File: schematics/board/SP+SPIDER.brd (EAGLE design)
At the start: 82 x 100 mm, 45 parts

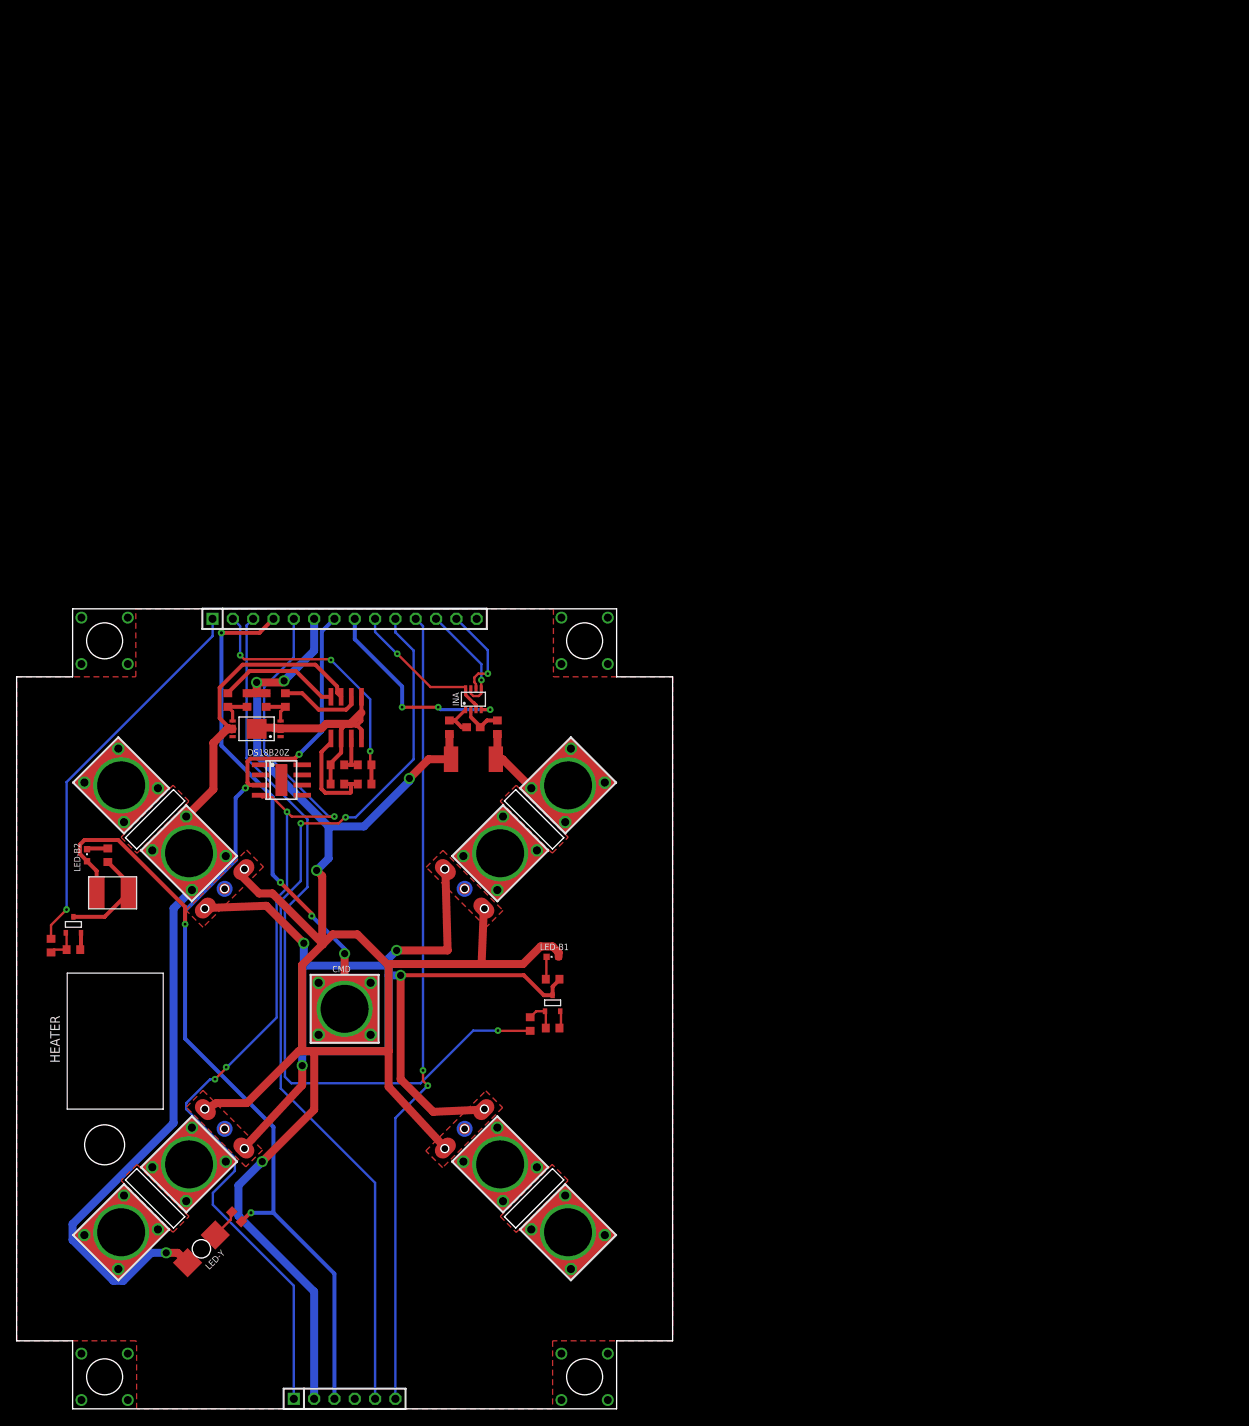
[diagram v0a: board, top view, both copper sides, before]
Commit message: Исправлены площадки механизмов Розе, соответствующие платы и герберы плат
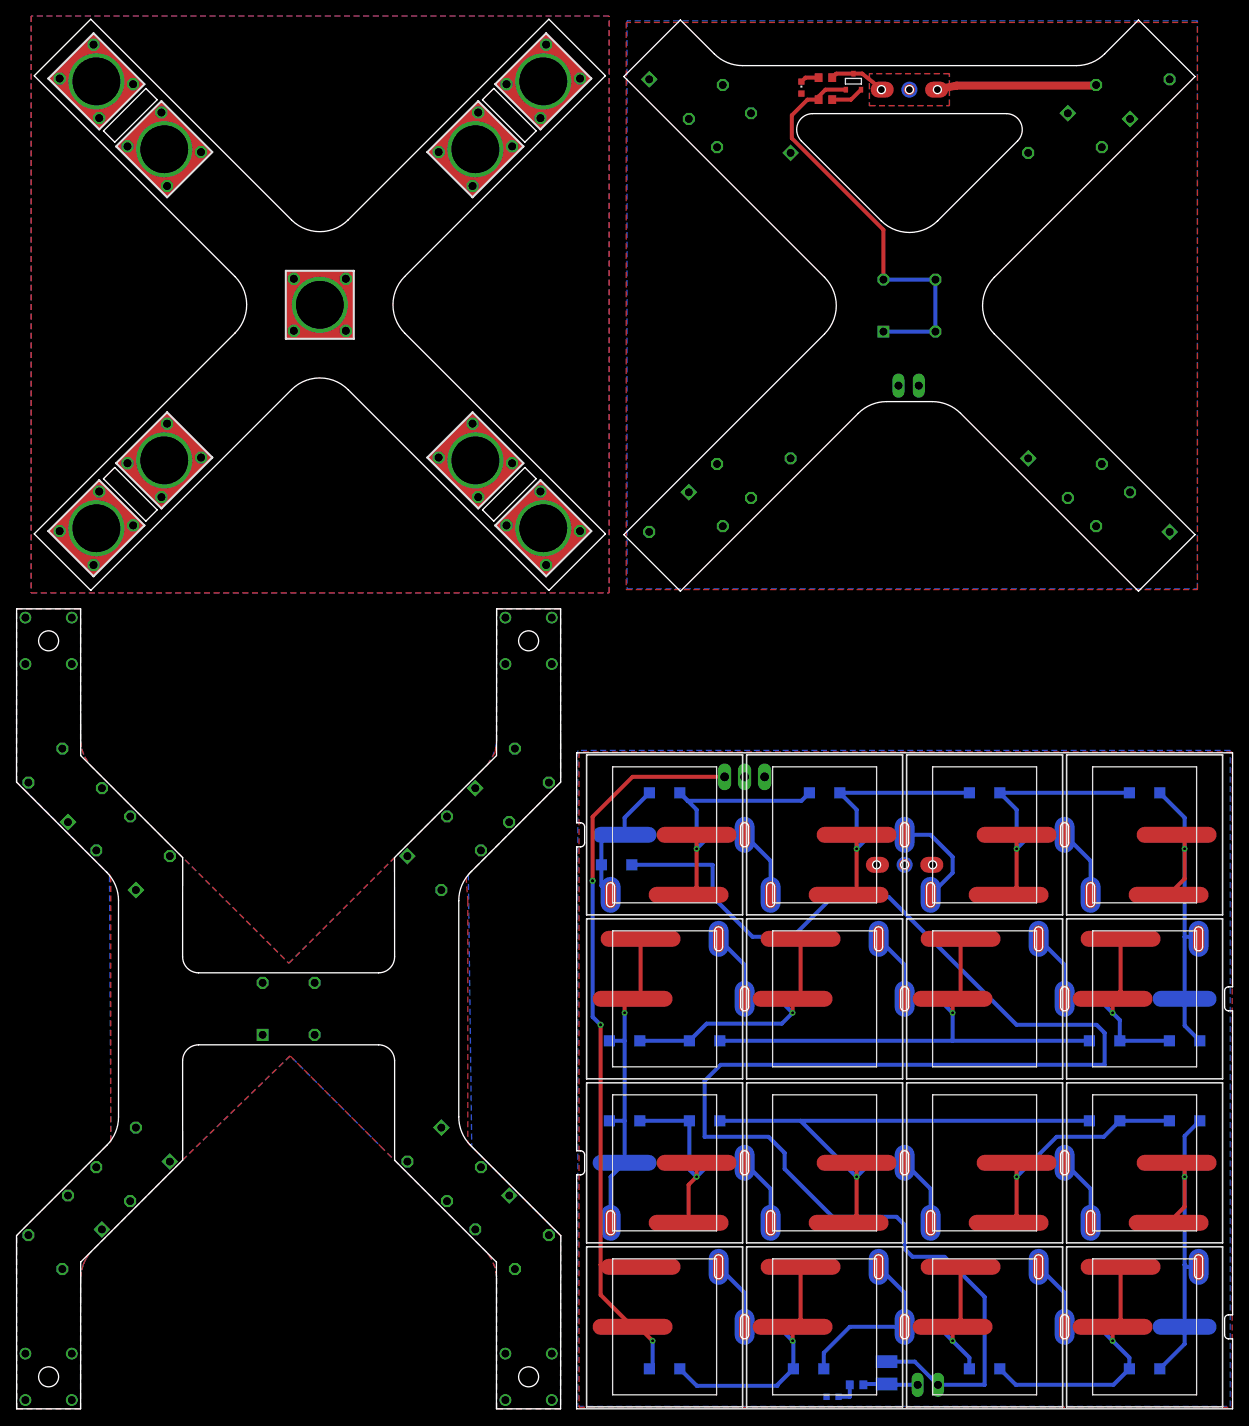
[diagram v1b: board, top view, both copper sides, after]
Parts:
- removed BKU: (no value), pinheadCS:1X14
- removed BSK5: (no value), pinheadCS:1X06
- removed C41: 0,1µ, rcl:C0603
- removed CMD: KCONNECTQUAD, CanCubeSat:KCONNECT_QUAD
- removed DS18B20Z: DS18B20Z, CanCubeSat:SOIC8+HEAT_S
- removed INA: INA219AID, CanCubeSat:SOT23-8
- removed LED-B1, LED-B2: (no value), led:CHIPLED_0603
- removed LED-Y: LAP4-BOTTOM, led:P47F-BOTTOM
- removed R12, R6: 100k, resistor:R0603
- removed R13: 1k5, resistor:R0603
- removed R14, R8: 1M, resistor:R0603
- removed R3, R32, R5, R9: 100R, resistor:R0603
- removed R4, R7: 2k, resistor:R0603
- removed R75: R01, rcl:R2512
- removed R76, R77: 10R, resistor:R0603
- removed R94, R95: 200k, resistor:R0603
- removed U$13, U$8: SI2302CDS, CanCubeSat:SOT23-3
- removed U$14: EM_HEAT, CanCubeSat:EM_HEAT
- removed U$15, U$16: GRAFITGRAFIT4_2, CanCubeSat:GRAFIT4_2
- removed U$9: PCB "BSK3", CanCubeSat:ITS-LOGO
- added 2K7: 2k7, rcl:R0603
- added C1: 47µ, rcl:C1210
- added D1, D10, D11, D12, D13, D14, D15, D16, D17, D2, D3, D4, D5, D6, D7, D8, D9: MBR0520LT, diode:SOD123
- added JP1, JP3: (no value), pinhead:1X02
- added LED1, PWR: (no value), led:CHIPLED_0603
- added S1: (no value), CanCubeSat:255SB
- added SOL1, SOL10, SOL11, SOL13, SOL14, SOL15, SOL2, SOL3, SOL5, SOL6, SOL7, SOL9: SOLAR-2_0, CanCubeSat:SOLAR_0-2
- added SOL12, SOL16, SOL4, SOL8: SOLAR-2_1, CanCubeSat:SOLAR_1-2
- added U$17, U$22, U$23, U$24, U$25, U$27, U$28: KCONNECT, CanCubeSat:KCONNECT
- added U$29: KCONNECTQUAD, CanCubeSat:KCONNECT_QUAD
- added U$32, U$33, U$38, U$39: KCONNECT3, CanCubeSat:KCONNECT-3
- added U$34, U$35, U$36: KCONNECT4, CanCubeSat:KCONNECT-4
- added U$37: KCONNECT1, CanCubeSat:KCONNECT-1
- added U$40: SI2302CDS, CanCubeSat:SOT23-3
- added U$41: GRAFITGRAFIT4_2, CanCubeSat:GRAFIT4_2
- added U$42: KCONNECTQUAD-, CanCubeSat:KCONNECT-_QUAD
- R1: value 2k26 -> 1k5
- R2: value 2k26 -> 1M
- U$1, U$18, U$19, U$2, U$20, U$21, U$3, U$4: value KCONNECT -> KCONNECT-; device CanCubeSat:KCONNECT -> CanCubeSat:KCONNECT-
- U$26: value FS8205A+ -> KCONNECT; device CanCubeSat:FS8205A+ -> CanCubeSat:KCONNECT
- U$5: value MOCD -> KCONNECTQUAD-; device CanCubeSat:SOIC8 -> CanCubeSat:KCONNECT-_QUAD
- U$7: value GRAFITGRAFIT4_2 -> PCB "Solar Panel"; device CanCubeSat:GRAFIT4_2 -> CanCubeSat:ITS-LOGO
- moved R1 105.4 mm to (101.1, 166.4)
- moved R2 101.2 mm to (101.1, 163.7)
- moved U$6 85.1 mm to (111.0, 68.0), turned to 90 degrees
- moved U$7 56.0 mm to (80.0, 50.0), flipped to the bottom, turned to 90 degrees
- moved U$26 43.3 mm to (57.3, 118.6), turned to 225 degrees
- moved U$5 37.1 mm to (34.0, 50.0)
- moved U$1 7.00 mm to (6.07, 77.9)
- moved U$18 7.00 mm to (6.07, 22.1)
- moved U$19 7.00 mm to (14.6, 30.6)
- moved U$2 7.00 mm to (14.6, 69.4)
- moved U$20 7.00 mm to (61.9, 22.1)
- moved U$21 7.00 mm to (53.4, 30.6)
- moved U$3 7.00 mm to (61.9, 77.9)
- moved U$4 7.00 mm to (53.4, 69.4)
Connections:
- removed net 1W: BKU.5, BSK5.1, DS18B20Z.4
- removed net 2: R13.2, U$13.3, U$15.P$1, U$15.P$4, U$16.P$1, U$16.P$4, U$6.P$1, U$6.P$4, U$7.P$1, U$7.P$4
- removed net 3V3: BKU.8, INA.4
- removed net 5V: BKU.7, BSK5.3, DS18B20Z.3, LED-B2.A, R4.1, U$14.1
- removed net B3-CMD: BKU.4, CMD.1, CMD.2, CMD.3, CMD.4, CMD.P$1, CMD.P$2
- removed net B3-KHEAT: BKU.1, R32.2
- removed net B3-KVCC: BKU.2, R1.2, R2.2
- removed net B3-ROZE: BKU.3, R3.2
- removed net B5-KHEAT: BKU.10, BSK5.5
- removed net GND: BKU.14, BKU.9, BSK5.4, DS18B20Z.5, DS18B20Z.HEAT, INA.3, INA.8, R14.2, R8.2, R94.1, R95.1, U$13.2, U$26.23, U$26.HEAT, U$5.2, U$5.4, U$5.5, U$8.2
- removed net N$150: C41.1, INA.1, R76.2
- removed net N$151: C41.2, INA.2, R77.2
- removed net N$20: R32.1, R8.1, U$8.1
- removed net N$21: R14.1, R3.1, U$13.1
- removed net OC1: R9.2, U$5.6
- removed net OD1: R5.2, U$5.8
- removed net SCL-TM: BKU.12, INA.5, INA.7
- removed net SDA-TM: BKU.13, INA.6
- removed net SINS-KVCC: BKU.11, BSK5.6
- removed net SP+: R75.1, R77.1, U$3.1, U$3.2, U$3.3, U$3.4, U$3.P$1, U$3.P$2
- removed net SP+1: U$1.1, U$1.2, U$1.3, U$1.4, U$1.P$1, U$1.P$2
- removed net SP+2: U$18.1, U$18.2, U$18.3, U$18.4, U$18.P$1, U$18.P$2
- removed net SP+3: U$20.1, U$20.2, U$20.3, U$20.4, U$20.P$1, U$20.P$2
- removed net SP-: LED-Y.C, U$2.1, U$2.2, U$2.3, U$2.4, U$2.P$1, U$2.P$2, U$26.67, U$5.7
- removed net SP-1: U$4.1, U$4.2, U$4.3, U$4.4, U$4.P$1, U$4.P$2
- removed net SP-2: U$19.1, U$19.2, U$19.3, U$19.4, U$19.P$1, U$19.P$2
- removed net SP-3: U$21.1, U$21.2, U$21.3, U$21.4, U$21.P$1, U$21.P$2
- new net BUS+1: 2K7.1, C1.2, JP1.2, S1.2
- new net BUS+2: U$17.1, U$17.2, U$17.3, U$17.4, U$17.P$1, U$17.P$2, U$22.1, U$22.2, U$22.3, U$22.4, U$22.P$1, U$22.P$2, U$25.1, U$25.2, U$25.3, U$25.4, U$25.P$1, U$25.P$2, U$27.1, U$27.2, U$27.3, U$27.4, U$27.P$1, U$27.P$2
- new net BUS+4: JP3.2, LED1.A, U$32.1, U$32.2, U$32.4, U$34.1, U$34.2, U$34.3, U$36.1, U$36.2, U$36.3, U$38.1, U$38.2, U$38.4, U$41.P$2, U$41.P$5
- new net BUS-: U$19.1, U$19.2, U$19.3, U$19.4, U$2.1, U$2.2, U$2.3, U$2.4, U$21.1, U$21.2, U$21.3, U$21.4, U$4.1, U$4.2, U$4.3, U$4.4
- new net BUS-1: C1.1, D1.C, JP1.1, PWR.C
- new net BUS-3: JP3.1, U$33.1, U$33.2, U$33.4, U$35.1, U$35.2, U$35.3, U$37.2, U$37.3, U$37.4, U$39.1, U$39.2, U$39.4
- new net CMD: U$5.1, U$5.2, U$5.3, U$5.4
- new net CMD1: U$29.1, U$29.2, U$29.3, U$29.4, U$29.P$1, U$29.P$2
- new net GND1: R2.2, U$40.2
- new net N$22: D12.A, D13.C, SOL5.OUT, SOL5.OUT-2, SOL5.OUT-21, SOL5.OUT1, SOL6.IN, SOL6.IN-2
- new net N$23: D11.A, D12.C, SOL6.OUT, SOL6.OUT-2, SOL6.OUT-21, SOL6.OUT1, SOL7.IN, SOL7.IN-2
- new net N$24: D13.A, D14.C, SOL4.OUT, SOL4.OUT-2, SOL4.OUT-21, SOL5.IN, SOL5.IN-2
- new net N$25: D10.A, D11.C, SOL7.OUT, SOL7.OUT-2, SOL7.OUT-21, SOL7.OUT1, SOL8.IN, SOL8.IN-2
- new net N$26: D10.C, D9.A, SOL8.OUT, SOL8.OUT-2, SOL8.OUT-21, SOL9.IN, SOL9.IN-2
- new net N$30: D5.A, D6.C, SOL12.OUT, SOL12.OUT-2, SOL12.OUT-21, SOL13.IN, SOL13.IN-2
- new net N$32: D3.A, D4.C, SOL14.OUT, SOL14.OUT-2, SOL14.OUT-21, SOL14.OUT1, SOL15.IN, SOL15.IN-2
- new net N$33: D2.A, D3.C, SOL15.OUT, SOL15.OUT-2, SOL15.OUT-21, SOL15.OUT1, SOL16.IN, SOL16.IN-2
- new net N$34: D1.A, D2.C, SOL16.OUT, SOL16.OUT-2, SOL16.OUT-21
- new net N$35: 2K7.2, PWR.A
- new net N$37: LED1.C, R1.1
- new net N$8: D15.A, D16.C, SOL2.OUT, SOL2.OUT-2, SOL2.OUT-21, SOL2.OUT1, SOL3.IN, SOL3.IN-2
- new net N$9: D14.A, D15.C, SOL3.OUT, SOL3.OUT-2, SOL3.OUT-21, SOL3.OUT1, SOL4.IN, SOL4.IN-2
- new net ROZE1: R2.1, U$40.1, U$42.1, U$42.2, U$42.3, U$42.4
- net 1: now also R1.2, U$40.3, U$41.P$1, U$41.P$4; no longer R7.2, U$14.2, U$8.3
- net BUS+: now also U$1.1, U$1.2, U$1.3, U$1.4, U$18.1, U$18.2, U$18.3, U$18.4, U$20.1, U$20.2, U$20.3, U$20.4, U$3.1, U$3.2, U$3.3, U$3.4; no longer BKU.6, BSK5.2, LED-B1.A, R12.2, R6.1, R75.2, R76.1, U$15.P$2, U$15.P$5, U$16.P$2, U$16.P$5, U$6.P$2, U$6.P$5, U$7.P$2, U$7.P$5
- net N$1: now also D17.A, S1.3, SOL1.IN, SOL1.IN-2; no longer R5.1, R6.2, U$26.5
- net N$2: now also U$23.1, U$23.2, U$23.3, U$23.4, U$23.P$1, U$23.P$2, U$24.1, U$24.2, U$24.3, U$24.4, U$24.P$1, U$24.P$2, U$26.1, U$26.2, U$26.3, U$26.4, U$26.P$1, U$26.P$2, U$28.1, U$28.2, U$28.3, U$28.4, U$28.P$1, U$28.P$2; no longer R1.1, R94.2, U$5.1
- net N$27: now also D8.A, D9.C, SOL10.IN, SOL10.IN-2, SOL9.OUT, SOL9.OUT-2, SOL9.OUT-21, SOL9.OUT1; no longer R12.1, R9.1, U$26.4
- net N$28: now also D7.A, D8.C, SOL10.OUT, SOL10.OUT-2, SOL10.OUT-21, SOL10.OUT1, SOL11.IN, SOL11.IN-2; no longer LED-Y.A, R4.2
- net N$29: now also D6.A, D7.C, SOL11.OUT, SOL11.OUT-2, SOL11.OUT-21, SOL11.OUT1, SOL12.IN, SOL12.IN-2; no longer LED-B1.C, R13.1
- net N$3: now also D16.A, D17.C, SOL1.OUT, SOL1.OUT-2, SOL1.OUT-21, SOL1.OUT1, SOL2.IN, SOL2.IN-2; no longer R2.1, R95.2, U$5.3
- net N$31: now also D4.A, D5.C, SOL13.OUT, SOL13.OUT-2, SOL13.OUT-21, SOL13.OUT1, SOL14.IN, SOL14.IN-2; no longer LED-B2.C, R7.1
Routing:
- net BUS+: track 248.4 -> 0.00 mm, vias 5 -> 0
- net BUS-1: track 0.00 -> 206.9 mm
- net 5V: track 148.3 -> 0.00 mm, vias 4 -> 0
- net 2: track 142.9 -> 0.00 mm, vias 4 -> 0
- net 1W: track 127.5 -> 0.00 mm, vias 4 -> 0
- net SP-: track 125.8 -> 0.00 mm, vias 1 -> 0
- net B5-KHEAT: track 113.8 -> 0.00 mm, vias 2 -> 0
- net SINS-KVCC: track 99.8 -> 0.00 mm, vias 2 -> 0
- net B3-ROZE: track 95.6 -> 0.00 mm, vias 1 -> 0
- net N$1: track 4.42 -> 96.5 mm, vias 0 -> 3
- net N$23: track 0.00 -> 79.6 mm, vias 0 -> 1
- net B3-CMD: track 79.0 -> 0.00 mm, vias 4 -> 0
- net N$28: track 3.72 -> 75.2 mm, vias 0 -> 1
- net GND: track 65.5 -> 0.00 mm, vias 1 -> 0
- net N$32: track 0.00 -> 54.1 mm, vias 0 -> 1
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- added copper zone on layer 16, net BUS+
- added copper zone on layer 1, net BUS+1
- added copper zone on layer 16, net BUS+2
- added copper zone on layer 1, net BUS+4
- added copper zone on layer 1, net BUS-
- added copper zone on layer 16, net BUS-1
- added copper zone on layer 16, net BUS-3
- added copper zone on layer 1, net N$2
- removed copper zone on layer 1, net GND
- removed copper zone on layer 1, net GND1
- removed copper zone on layer 1, net GND2
- removed copper zone on layer 1, net GND3
- removed copper zone on layer 1, net GND4
- removed copper zone on layer 1, net HEAT1
- removed copper zone on layer 1, net HEAT2
- removed copper zone on layer 1, net HEAT3
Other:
- board size 82 x 100 mm -> 152 x 173.7 mm
- board text added: "OFF"
- board text added: "ON"
- board text removed: "HEATER"
- board text removed: "to BKU"
- board text removed: "to BSK5"
